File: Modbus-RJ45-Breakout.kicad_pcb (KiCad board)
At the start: 2 copper layers, 87 x 68 mm, 99 parts, among them J1 RJ45_Weidmueller_2562920000, J2 RJ45_Weidmueller_2562920000, J3 Conn_01x04, J4 Conn_01x04, J5 USB_B_Mini, J6 2X04, Q1 BSP250, U1 FT2232D, U2 WE-TVS-82400102, U3 MAX485E, U4 ADM2687E, U5 93LC46B, U6 WE-TVS-82400102, U7 MAX485E, U8 ADM2687E, Y1 6MHz

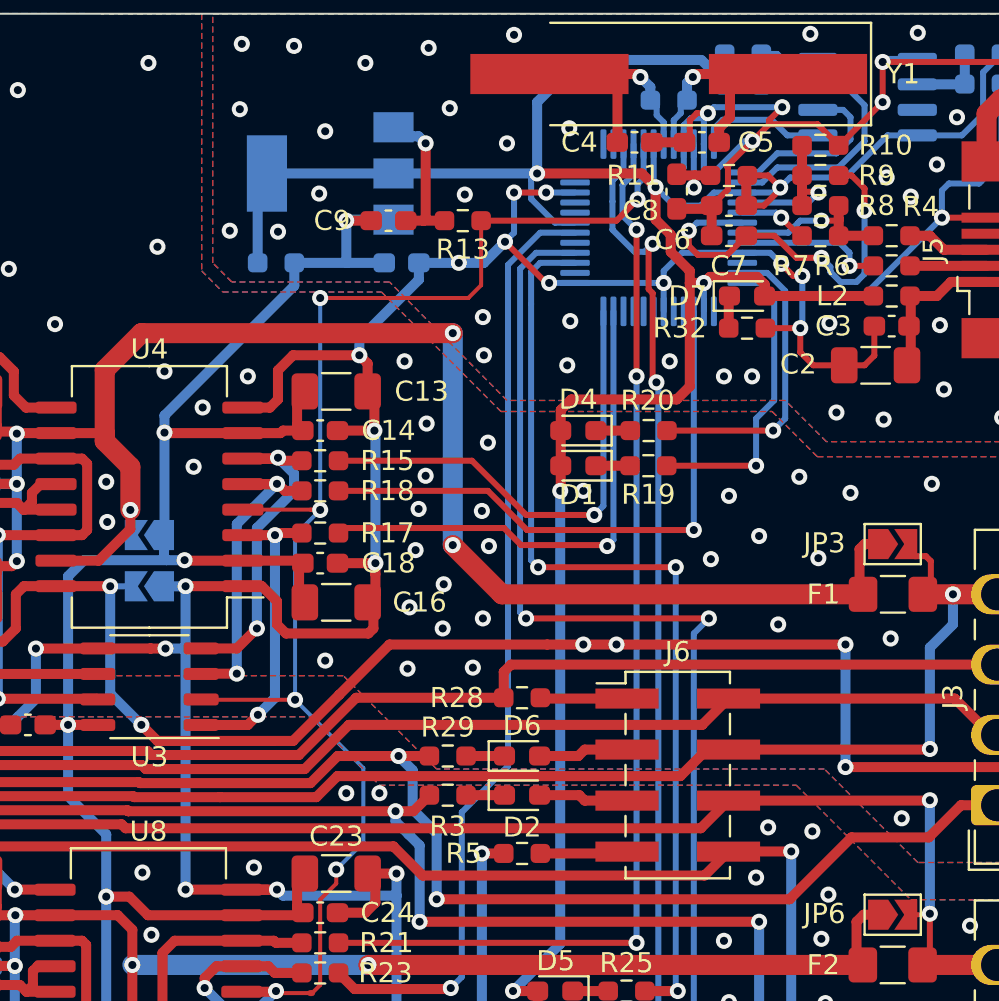
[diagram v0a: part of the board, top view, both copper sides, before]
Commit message: Moved the USB-Power LED to a more central position
Since many cases have their clear view window in the center,
I moved the USB Power LED also there to be easily visible.
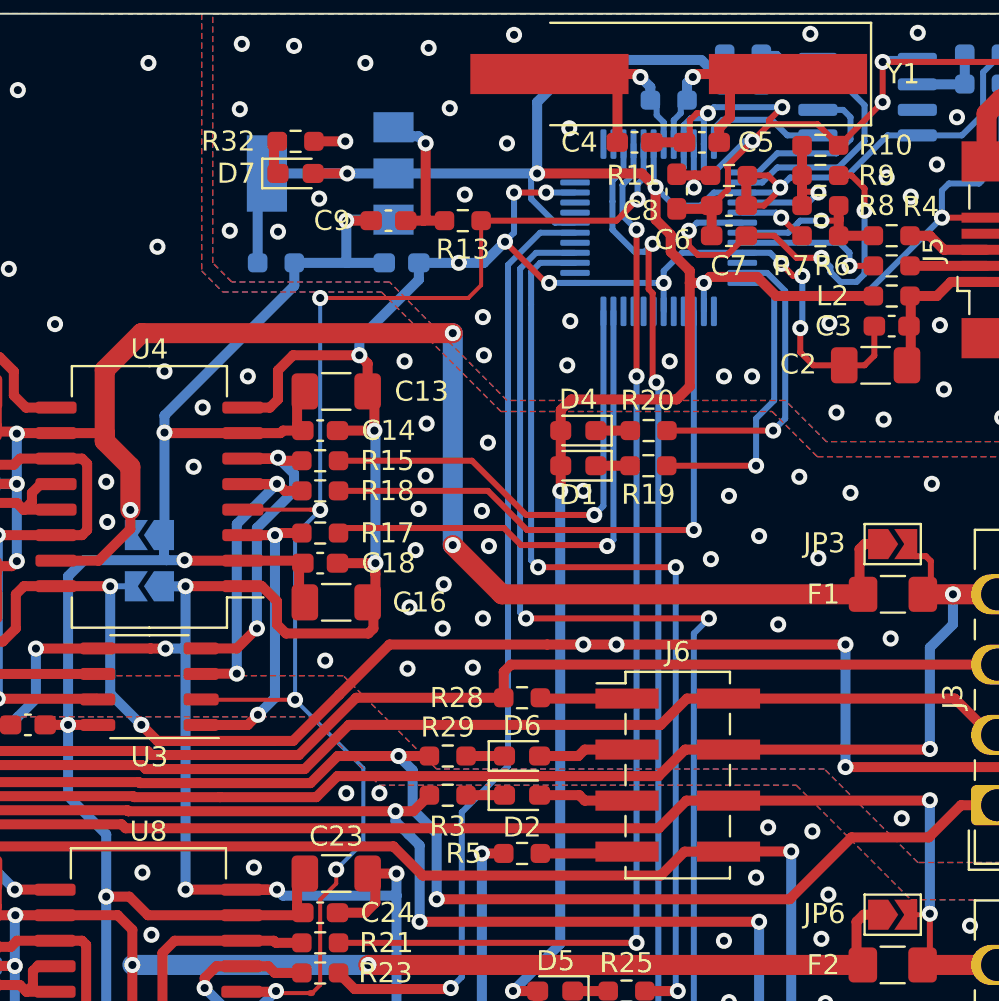
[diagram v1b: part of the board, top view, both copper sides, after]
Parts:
- moved R32 24.3 mm to (95.2, 56.4)
- moved D7 23.3 mm to (95.2, 58.0)
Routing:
- net VCC: track 134.1 -> 135.5 mm, vias 6 -> 7

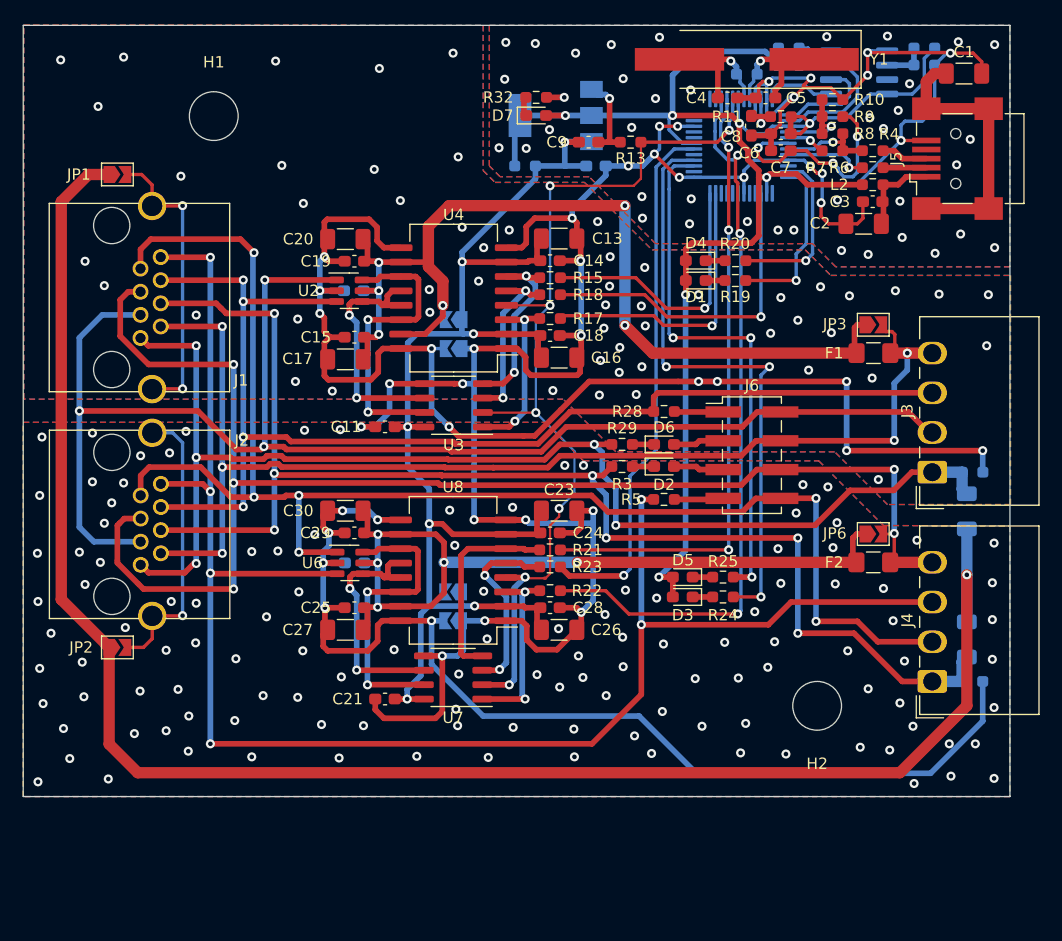
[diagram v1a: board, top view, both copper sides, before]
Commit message: Partly improved and re-routed
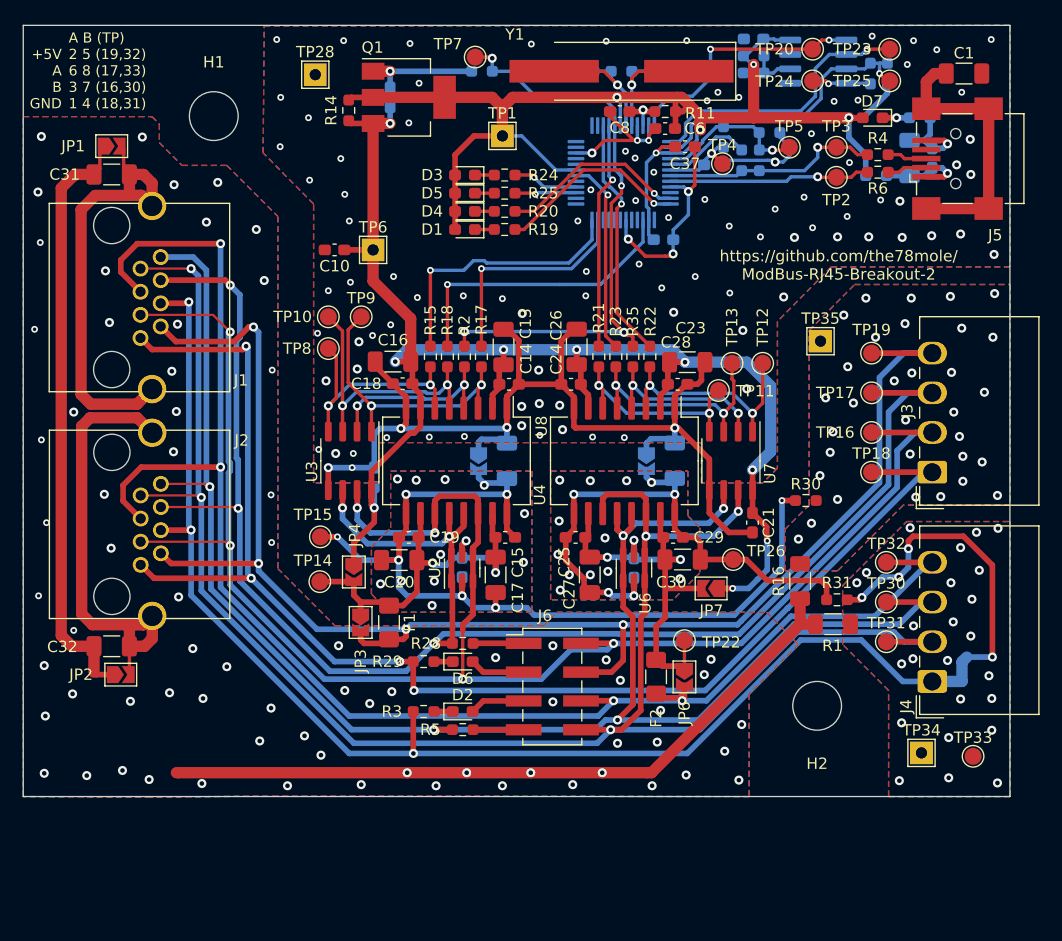
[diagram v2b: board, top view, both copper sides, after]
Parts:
- added C31: 1n, Capacitor_SMD:C_1206_3216Metric_Pad1.33x1.80mm_HandSolder, F.Cu at (57.8, 63.1)
- added C32: 1n, Capacitor_SMD:C_1206_3216Metric_Pad1.33x1.80mm_HandSolder, F.Cu at (57.8, 104.8)
- added C33: 1n, Capacitor_SMD:C_1206_3216Metric_Pad1.33x1.80mm_HandSolder, B.Cu at (92.7, 88.4)
- added C34: 1n, Capacitor_SMD:C_1206_3216Metric_Pad1.33x1.80mm_HandSolder, B.Cu at (107.5, 88.4)
- added C35: 100n, Capacitor_SMD:C_0603_1608Metric_Pad1.08x0.95mm_HandSolder, B.Cu at (114.4, 51.2)
- added C36: 100n, Capacitor_SMD:C_0603_1608Metric_Pad1.08x0.95mm_HandSolder, B.Cu at (106.5, 68.9)
- added C37: 100n, Capacitor_SMD:C_0603_1608Metric_Pad1.08x0.95mm_HandSolder, F.Cu at (108.3, 60.7)
- added R2: 27, Resistor_SMD:R_0603_1608Metric_Pad0.98x0.95mm_HandSolder, F.Cu at (88.9, 79.2)
- added R35: 27, Resistor_SMD:R_0603_1608Metric_Pad0.98x0.95mm_HandSolder, F.Cu at (103.8, 79.2)
- added TP1: Probe, TestPoint:TestPoint_THTPad_2.0x2.0mm_Drill1.0mm, F.Cu at (92.2, 59.8)
- added TP10: Probe, TestPoint:TestPoint_Pad_D1.5mm, F.Cu at (76.9, 75.7)
- added TP11: Probe, TestPoint:TestPoint_Pad_D1.5mm, F.Cu at (111.3, 82.2)
- added TP12: Probe, TestPoint:TestPoint_Pad_D1.5mm, F.Cu at (115.2, 79.8)
- added TP13: Probe, TestPoint:TestPoint_Pad_D1.5mm, F.Cu at (112.5, 79.8)
- added TP14: Probe, TestPoint:TestPoint_Pad_D1.5mm, F.Cu at (76.2, 99.0)
- added TP15: Probe, TestPoint:TestPoint_Pad_D1.5mm, F.Cu at (76.2, 95.1)
- added TP16: Probe, TestPoint:TestPoint_Pad_D1.5mm, F.Cu at (124.8, 85.9)
- added TP17: Probe, TestPoint:TestPoint_Pad_D1.5mm, F.Cu at (124.8, 82.4)
- added TP18: Probe, TestPoint:TestPoint_Pad_D1.5mm, F.Cu at (124.8, 89.4)
- added TP19: Probe, TestPoint:TestPoint_Pad_D1.5mm, F.Cu at (124.8, 78.9)
- added TP2: Probe, TestPoint:TestPoint_Pad_D1.5mm, F.Cu at (121.7, 63.4)
- added TP20: Probe, TestPoint:TestPoint_Pad_D1.5mm, F.Cu at (119.6, 52.1)
- added TP22: Probe, TestPoint:TestPoint_Pad_D1.5mm, F.Cu at (108.3, 104.2)
- added TP23: Probe, TestPoint:TestPoint_Pad_D1.5mm, F.Cu at (126.4, 52.1)
- added TP24: Probe, TestPoint:TestPoint_Pad_D1.5mm, F.Cu at (119.6, 54.9)
- added TP25: Probe, TestPoint:TestPoint_Pad_D1.5mm, F.Cu at (126.4, 54.9)
- added TP26: Probe, TestPoint:TestPoint_Pad_D1.5mm, F.Cu at (112.6, 97.1)
- added TP28: Probe, TestPoint:TestPoint_THTPad_2.0x2.0mm_Drill1.0mm, F.Cu at (75.8, 54.4)
- added TP3: Probe, TestPoint:TestPoint_Pad_D1.5mm, F.Cu at (121.7, 60.8)
- added TP30: Probe, TestPoint:TestPoint_Pad_D1.5mm, F.Cu at (126.1, 100.8)
- added TP31: Probe, TestPoint:TestPoint_Pad_D1.5mm, F.Cu at (126.1, 104.3)
- added TP32: Probe, TestPoint:TestPoint_Pad_D1.5mm, F.Cu at (126.1, 97.3)
- added TP33: Probe, TestPoint:TestPoint_Pad_D1.5mm, F.Cu at (133.8, 114.5)
- added TP34: Probe, TestPoint:TestPoint_THTPad_2.0x2.0mm_Drill1.0mm, F.Cu at (129.2, 114.2)
- added TP35: Probe, TestPoint:TestPoint_THTPad_2.0x2.0mm_Drill1.0mm, F.Cu at (120.3, 77.8)
- added TP4: Probe, TestPoint:TestPoint_Pad_D1.5mm, F.Cu at (111.7, 62.2)
- added TP5: Probe, TestPoint:TestPoint_Pad_D1.5mm, F.Cu at (117.5, 60.8)
- added TP6: Probe, TestPoint:TestPoint_THTPad_2.0x2.0mm_Drill1.0mm, F.Cu at (80.8, 69.8)
- added TP7: Probe, TestPoint:TestPoint_Pad_D1.5mm, F.Cu at (89.8, 52.8)
- added TP8: Probe, TestPoint:TestPoint_Pad_D1.5mm, F.Cu at (76.9, 78.5)
- added TP9: Probe, TestPoint:TestPoint_Pad_D1.5mm, F.Cu at (79.8, 75.7)
- C10, JP4, JP7, Q1, R1, R14, R16, R30, R31: moved to F.Cu
- C11, C2, C3, C4, C5, C7, C9, L2, R10, R13, R32, R7, R8, R9: moved to B.Cu
- moved JP3 52.3 mm to (79.8, 102.7), turned to -90 degrees
- moved F1 48.9 mm to (82.2, 102.7), turned to -90 degrees
- moved R24 41.9 mm to (92.5, 63.2)
- moved D3 41.9 mm to (89.0, 63.2)
- moved R25 38.9 mm to (92.5, 64.8)
- moved D5 38.9 mm to (89.0, 64.8)
- moved C21 35.9 mm to (114.3, 93.8), turned to -90 degrees
- moved R32 33.9 mm to (129.1, 58.1)
- moved U7 31.1 mm to (112.4, 88.4), turned to -90 degrees
- moved C30 30.0 mm to (108.1, 97.1), turned to 0 degrees
- moved D7 29.7 mm to (124.9, 58.1), turned to 180 degrees
- moved C20 28.7 mm to (83.2, 97.2)
- moved C29 28.1 mm to (107.3, 95.2), turned to 0 degrees
- moved D2 28.0 mm to (88.8, 110.5)
- moved R3 27.8 mm to (85.3, 110.5)
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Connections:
- net Net-(C2-Pad1) renamed /VBUS
- U2 pad 1: /B_1 -> /A_1
- U2 pad 3: /A_1 -> /B_1
- U2 pad 4: Net-(U2-Pad4) -> /B_1
- U2 pad 6: Net-(U2-Pad6) -> /A_1
- U3 pad 2: nPWREN -> Net-(R2-Pad1)
- U3 pad 6: Net-(U2-Pad4) -> /A_1
- U3 pad 7: Net-(U2-Pad6) -> /B_1
- U4 pad 11: Net-(U2-Pad6) -> /B_1
- U4 pad 12: Net-(U2-Pad4) -> /A_1
- U4 pad 13: Net-(U2-Pad4) -> /A_1
- U4 pad 14: Net-(U2-Pad6) -> /B_1
- U4 pad 4: nPWREN -> Net-(R2-Pad1)
- U6 pad 1: /B_2 -> /A_2
- U6 pad 3: /A_2 -> /B_2
- U6 pad 4: Net-(U6-Pad4) -> /B_2
- U6 pad 6: Net-(U6-Pad6) -> /A_2
- U7 pad 2: nPWREN -> Net-(R35-Pad1)
- U7 pad 6: Net-(U6-Pad4) -> /A_2
- U7 pad 7: Net-(U6-Pad6) -> /B_2
- U8 pad 11: Net-(U6-Pad6) -> /B_2
- U8 pad 12: Net-(U6-Pad4) -> /A_2
- U8 pad 13: Net-(U6-Pad4) -> /A_2
- U8 pad 14: Net-(U6-Pad6) -> /B_2
- U8 pad 4: nPWREN -> Net-(R35-Pad1)
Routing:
- net GND: track 245.9 -> 141.1 mm, vias 68 -> 105
- net Net-(C12-Pad1): track 88.4 -> 35.7 mm, vias 6 -> 3
- net GND2: track 100.5 -> 51.2 mm, vias 127 -> 16
- net Net-(R24-Pad1): track 52.7 -> 5.81 mm, vias 3 -> 1
- net /A_1: track 106.4 -> 152.5 mm, vias 4 -> 5
- net Net-(R22-Pad1): track 64.4 -> 21.5 mm, vias 3 -> 1
- net Net-(R25-Pad1): track 46.8 -> 5.48 mm, vias 3 -> 1
- net Net-(C22-Pad1): track 75.3 -> 38.6 mm, vias 5 -> 3
- net GNDS: track 153.7 -> 117.0 mm, vias 1 -> 72
- net Net-(R21-Pad1): track 55.1 -> 20.1 mm, vias 3 -> 1
- net nPWREN: track 84.7 -> 52.8 mm, vias 7 -> 4
- net /B_2: track 128.3 -> 158.4 mm, vias 6 -> 5
- net Net-(R23-Pad1): track 47.1 -> 17.3 mm
- net /+5V_1: track 106.7 -> 135.5 mm, vias 5 -> 4
- net /B_1: track 129.0 -> 156.9 mm, vias 3 -> 6
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- added copper zone on B.Cu, net /GND_1
- added copper zone on F.Cu, net /GND_1
- added copper zone on B.Cu, net /GND_2
- added copper zone on F.Cu, net /GND_2
- added copper zone on B.Cu, net GNDS
- added copper zone on F.Cu, net GNDS
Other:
- board text added: "+5V A B GND"
- board text added: "A B (TP) 2 5 (19,32) 6 8 (17,33) 3 7 (16,30) 1 4 (18,31)"
- board text added: "https://github.com/the78mole/ ModBus-RJ45-Breakout-2"

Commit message: As ordered, added info on enclosures
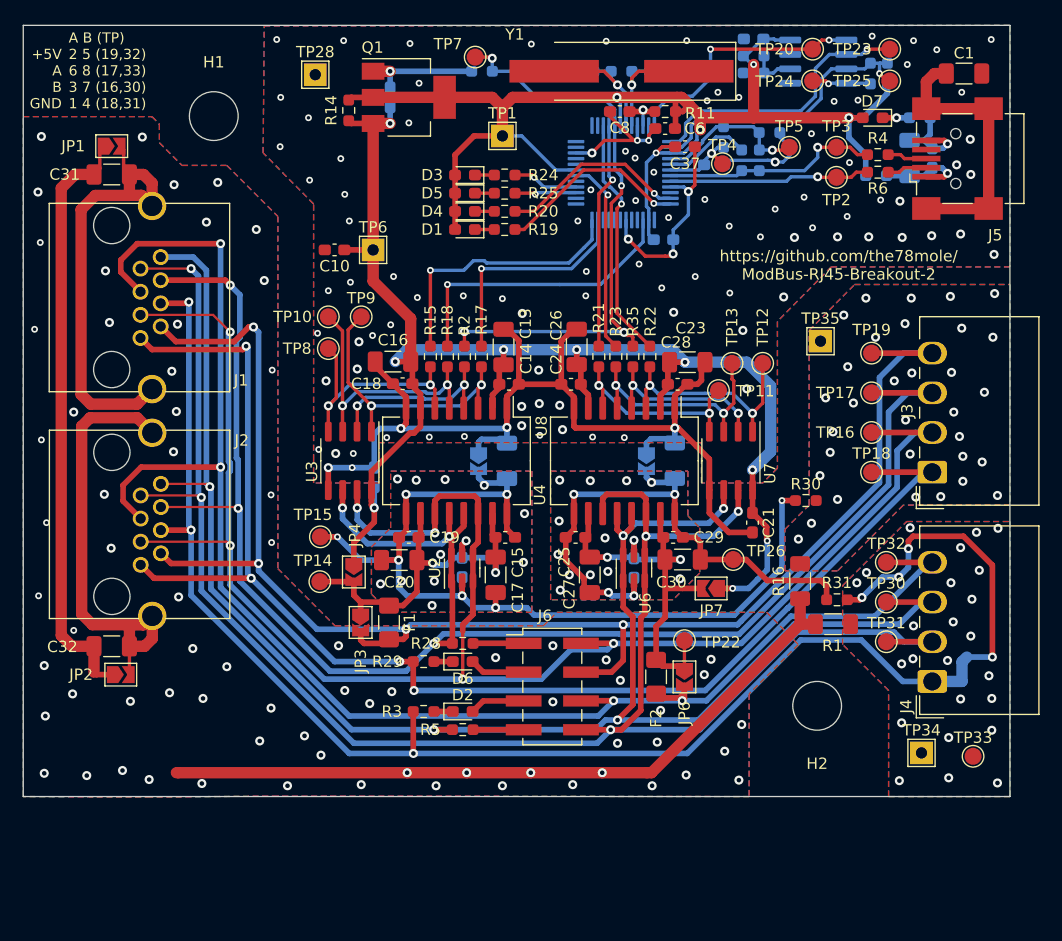
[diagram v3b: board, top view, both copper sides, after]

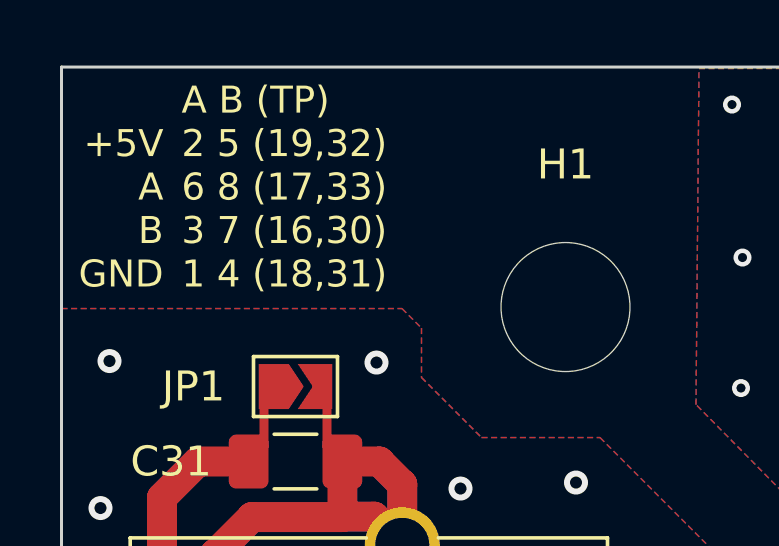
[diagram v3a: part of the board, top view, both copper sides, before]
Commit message: Fixed TP docs on PCB and added ibom
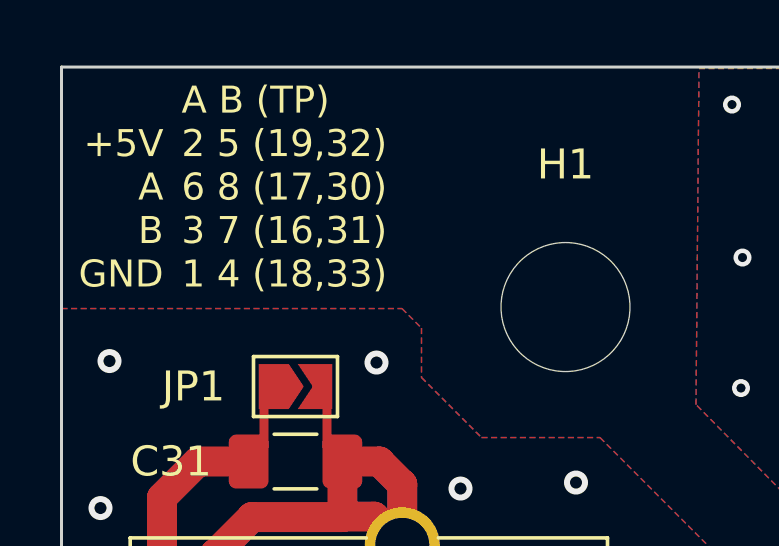
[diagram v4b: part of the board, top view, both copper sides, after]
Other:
- board text added: "A B (TP) 2 5 (19,32) 6 8 (17,30) 3 7 (16,31) 1 4 (18,33)"
- board text removed: "A B (TP) 2 5 (19,32) 6 8 (17,33) 3 7 (16,30) 1 4 (18,31)"
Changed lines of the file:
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@@
     (effects (font (size 1 1) (thickness 0.15)))
   )
-  (gr_text "A B (TP)\n2 5 (19,32)\n6 8 (17,33)\n3 7 (16,30)\n1 4 (18,31)\n" (at 54 54) (layer "F.SilkS")
+  (gr_text "A B (TP)\n2 5 (19,32)\n6 8 (17,30)\n3 7 (16,31)\n1 4 (18,33)\n" (at 54 54) (layer "F.SilkS")
     (effects (font (size 0.9 0.9) (thickness 0.16)) (justify left))
   )
